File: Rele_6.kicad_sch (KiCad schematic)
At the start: 5 parts

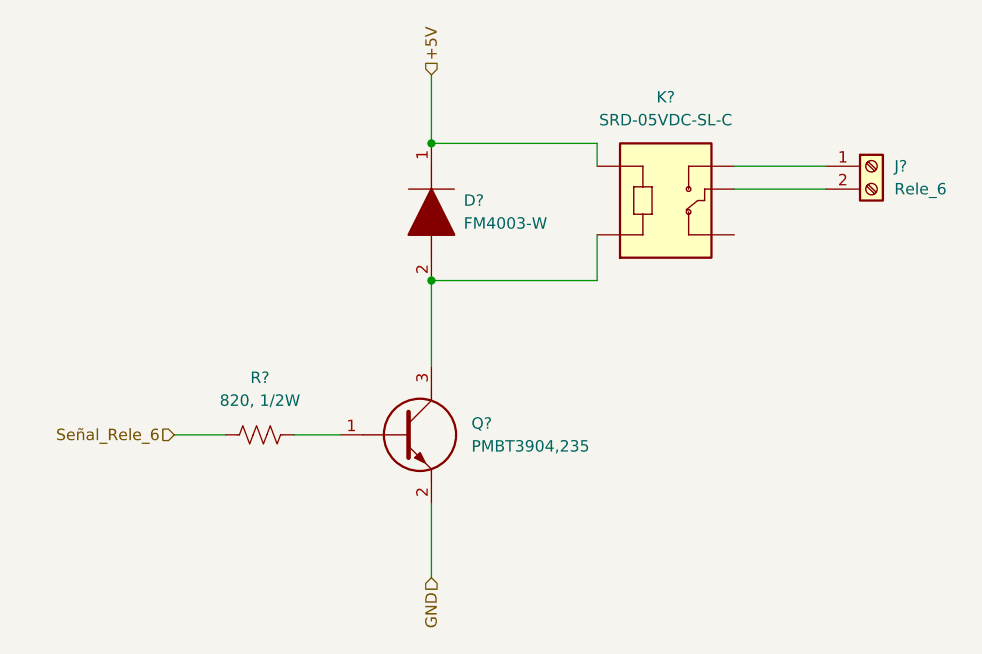
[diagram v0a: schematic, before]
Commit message: Ajuste del esquematico
Se cambio el integrado ESP32 por 2 tiras de pines de 1x15, se quitaron los switches EN y BOOT que ya estan en el NodeMCU, se quito el mutliplexor 74HC y se cablearon las I/O
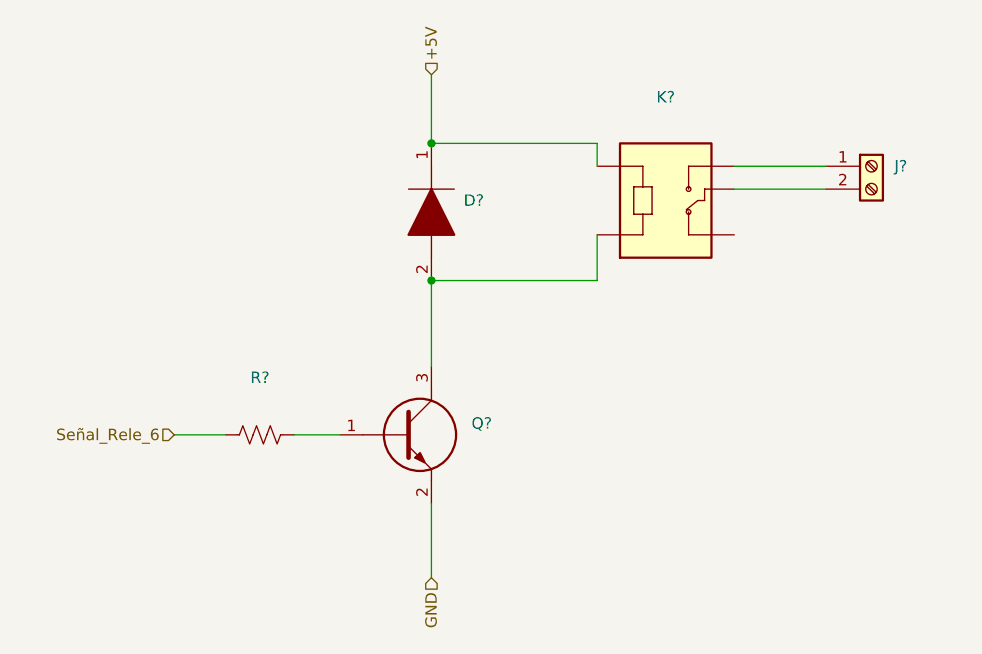
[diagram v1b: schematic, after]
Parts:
- D?: value FM4003-W -> (none); footprint DIOM5025X231N -> (none)
- J?: value Rele_6 -> (none)
- K?: value SRD-05VDC-SL-C -> (none); footprint RELAY_SRD-05VDC-SL-C -> (none)
- Q?: value PMBT3904,235 -> (none); footprint SOT95P230X110-3N -> (none)
- R?: value 820, 1/2W -> (none)
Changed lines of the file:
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@@
     (in_bom yes) (on_board yes) (fields_autoplaced)
     (property "Reference" "R?" (id 0) (at 127.635 100.965 90))
-    (property "Value" "820, 1/2W" (id 1) (at 127.635 103.505 90))
+    (property "Value" "" (id 1) (at 127.635 103.505 90))
     (property "Footprint" "" (id 2) (at 127.889 106.299 90)
       (effects (font (size 1.27 1.27)) hide)
@@
       (effects (font (size 1.27 1.27)) (justify left))
     )
-    (property "Value" "Rele_6" (id 1) (at 198.12 80.0099 0)
+    (property "Value" "" (id 1) (at 198.12 80.0099 0)
       (effects (font (size 1.27 1.27)) (justify left))
     )
@@
       (effects (font (size 1.27 1.27)) (justify left))
     )
-    (property "Value" "FM4003-W" (id 1) (at 150.2664 83.8199 90)
+    (property "Value" "" (id 1) (at 150.2664 83.8199 90)
       (effects (font (size 1.27 1.27)) (justify left))
     )
-    (property "Footprint" "DIOM5025X231N" (id 2) (at 146.685 86.36 0)
+    (property "Footprint" "" (id 2) (at 146.685 86.36 0)
       (effects (font (size 1.27 1.27)) (justify left) hide)
     )
@@
       (effects (font (size 1.27 1.27)) (justify left))
     )
-    (property "Value" "PMBT3904,235" (id 1) (at 151.13 108.5849 0)
+    (property "Value" "" (id 1) (at 151.13 108.5849 0)
       (effects (font (size 1.27 1.27)) (justify left))
     )
-    (property "Footprint" "SOT95P230X110-3N" (id 2) (at 150.495 111.125 0)
+    (property "Footprint" "" (id 2) (at 150.495 111.125 0)
       (effects (font (size 1.27 1.27)) (justify left) hide)
     )
@@
     (in_bom yes) (on_board yes) (fields_autoplaced)
     (property "Reference" "K?" (id 0) (at 172.72 69.7992 0))
-    (property "Value" "SRD-05VDC-SL-C" (id 1) (at 172.72 72.3392 0))
-    (property "Footprint" "RELAY_SRD-05VDC-SL-C" (id 2) (at 172.72 80.01 0)
+    (property "Value" "" (id 1) (at 172.72 72.3392 0))
+    (property "Footprint" "" (id 2) (at 172.72 80.01 0)
       (effects (font (size 1.27 1.27)) (justify left bottom) hide)
     )

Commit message: Modificación de posición de circ. filtrado y circ. de adaptación de tensión
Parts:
- D?, J?, K?, Q?, R?: value (none) -> ~
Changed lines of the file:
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@@
     (in_bom yes) (on_board yes) (fields_autoplaced)
     (property "Reference" "R?" (id 0) (at 127.635 100.965 90))
-    (property "Value" "" (id 1) (at 127.635 103.505 90))
+    (property "Value" "~" (id 1) (at 127.635 103.505 90))
     (property "Footprint" "" (id 2) (at 127.889 106.299 90)
       (effects (font (size 1.27 1.27)) hide)
@@
       (effects (font (size 1.27 1.27)) (justify left))
     )
-    (property "Value" "" (id 1) (at 198.12 80.0099 0)
+    (property "Value" "~" (id 1) (at 198.12 80.0099 0)
       (effects (font (size 1.27 1.27)) (justify left))
     )
@@
       (effects (font (size 1.27 1.27)) (justify left))
     )
-    (property "Value" "" (id 1) (at 150.2664 83.8199 90)
+    (property "Value" "~" (id 1) (at 150.2664 83.8199 90)
       (effects (font (size 1.27 1.27)) (justify left))
     )
@@
       (effects (font (size 1.27 1.27)) (justify left))
     )
-    (property "Value" "" (id 1) (at 151.13 108.5849 0)
+    (property "Value" "~" (id 1) (at 151.13 108.5849 0)
       (effects (font (size 1.27 1.27)) (justify left))
     )
@@
     (in_bom yes) (on_board yes) (fields_autoplaced)
     (property "Reference" "K?" (id 0) (at 172.72 69.7992 0))
-    (property "Value" "" (id 1) (at 172.72 72.3392 0))
+    (property "Value" "~" (id 1) (at 172.72 72.3392 0))
     (property "Footprint" "" (id 2) (at 172.72 80.01 0)
       (effects (font (size 1.27 1.27)) (justify left bottom) hide)

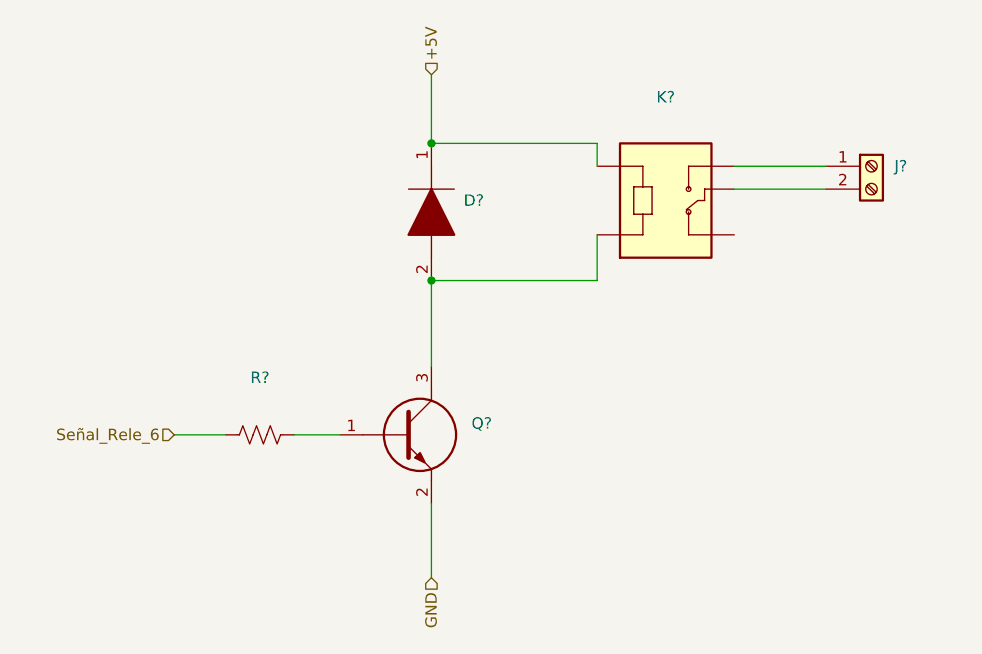
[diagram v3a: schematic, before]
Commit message: Actualización de SCH según placa industrial, y búsqueda de footprints.
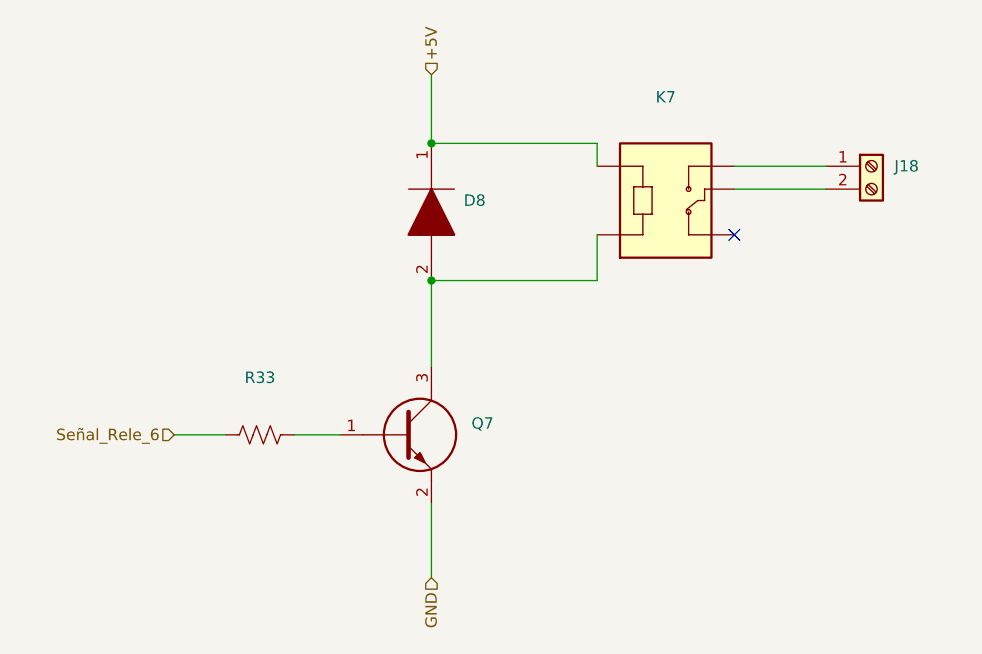
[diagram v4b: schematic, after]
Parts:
- D8: renamed from D?; value ~ -> (none)
- J18: renamed from J?; value ~ -> (none)
- K7: renamed from K?; value ~ -> (none)
- Q7: renamed from Q?; value ~ -> (none)
- R33: renamed from R?; value ~ -> (none)
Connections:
- no-connect marks 0 -> 1
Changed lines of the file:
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@@
   (junction (at 146.685 90.17) (diameter 0) (color 0 0 0 0)
   )
+  (no_connect (at 180.34 85.09))
   (wire (pts (xy 146.685 90.17) (xy 165.1 90.17))
     (stroke (width 0) (type default) (color 0 0 0 0))
@@
   (symbol (lib_id "Device:R_US") (at 127.635 107.315 90) (unit 1)
     (in_bom yes) (on_board yes) (fields_autoplaced)
-    (property "Reference" "R?" (id 0) (at 127.635 100.965 90))
-    (property "Value" "~" (id 1) (at 127.635 103.505 90))
+    (property "Reference" "R33" (id 0) (at 127.635 100.965 90))
+    (property "Value" "" (id 1) (at 127.635 103.505 90))
     (property "Footprint" "" (id 2) (at 127.889 106.299 90)
       (effects (font (size 1.27 1.27)) hide)
@@
   (symbol (lib_id "Connector:Screw_Terminal_01x02") (at 195.58 77.47 0) (unit 1)
     (in_bom yes) (on_board yes) (fields_autoplaced)
-    (property "Reference" "J?" (id 0) (at 198.12 77.4699 0)
+    (property "Reference" "J18" (id 0) (at 198.12 77.4699 0)
       (effects (font (size 1.27 1.27)) (justify left))
     )
-    (property "Value" "~" (id 1) (at 198.12 80.0099 0)
+    (property "Value" "" (id 1) (at 198.12 80.0099 0)
       (effects (font (size 1.27 1.27)) (justify left))
     )
@@
   (symbol (lib_id "FM4003-W:FM4003-W") (at 146.685 74.93 270) (unit 1)
     (in_bom yes) (on_board yes) (fields_autoplaced)
-    (property "Reference" "D?" (id 0) (at 150.2664 81.2799 90)
+    (property "Reference" "D8" (id 0) (at 150.2664 81.2799 90)
       (effects (font (size 1.27 1.27)) (justify left))
     )
-    (property "Value" "~" (id 1) (at 150.2664 83.8199 90)
+    (property "Value" "" (id 1) (at 150.2664 83.8199 90)
       (effects (font (size 1.27 1.27)) (justify left))
     )
@@
   (symbol (lib_id "PMBT3904,235:PMBT3904,235") (at 136.525 107.315 0) (unit 1)
     (in_bom yes) (on_board yes) (fields_autoplaced)
-    (property "Reference" "Q?" (id 0) (at 151.13 106.0449 0)
+    (property "Reference" "Q7" (id 0) (at 151.13 106.0449 0)
       (effects (font (size 1.27 1.27)) (justify left))
     )
-    (property "Value" "~" (id 1) (at 151.13 108.5849 0)
+    (property "Value" "" (id 1) (at 151.13 108.5849 0)
       (effects (font (size 1.27 1.27)) (justify left))
     )
@@
   (symbol (lib_id "SRD-05VDC-SL-C:SRD-05VDC-SL-C") (at 172.72 80.01 0) (unit 1)
     (in_bom yes) (on_board yes) (fields_autoplaced)
-    (property "Reference" "K?" (id 0) (at 172.72 69.7992 0))
-    (property "Value" "~" (id 1) (at 172.72 72.3392 0))
+    (property "Reference" "K7" (id 0) (at 172.72 69.7992 0))
+    (property "Value" "" (id 1) (at 172.72 72.3392 0))
     (property "Footprint" "" (id 2) (at 172.72 80.01 0)
       (effects (font (size 1.27 1.27)) (justify left bottom) hide)

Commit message: Fin de SCH, config de inicio para PCB
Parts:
- D8: value (none) -> FM4003-W; footprint (none) -> FM4003W:DIOM5025X231N
- J18: value (none) -> Rele_6; footprint (none) -> TB002-500-02BE:TB00250002BE
- K7: value (none) -> SRD-05VDC-SL-C; footprint (none) -> SRD-05VDC-SL-C-Version_2:RELAY_SRD-05VDC-SL-C
- Q7: value (none) -> PMBT3904,235; footprint (none) -> PMBT3904,235:SOT95P230X110-3N
- R33: value (none) -> 820, 1/2W; footprint (none) -> Resistor_SMD:R_0805_2012Metric
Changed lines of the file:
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@@
     (in_bom yes) (on_board yes) (fields_autoplaced)
     (property "Reference" "R33" (id 0) (at 127.635 100.965 90))
-    (property "Value" "" (id 1) (at 127.635 103.505 90))
-    (property "Footprint" "" (id 2) (at 127.889 106.299 90)
+    (property "Value" "820, 1/2W" (id 1) (at 127.635 103.505 90))
+    (property "Footprint" "Resistor_SMD:R_0805_2012Metric" (id 2) (at 127.889 106.299 90)
       (effects (font (size 1.27 1.27)) hide)
     )
@@
       (effects (font (size 1.27 1.27)) (justify left))
     )
-    (property "Value" "" (id 1) (at 198.12 80.0099 0)
+    (property "Value" "Rele_6" (id 1) (at 198.12 80.0099 0)
       (effects (font (size 1.27 1.27)) (justify left))
     )
-    (property "Footprint" "" (id 2) (at 195.58 77.47 0)
+    (property "Footprint" "TB002-500-02BE:TB00250002BE" (id 2) (at 195.58 77.47 0)
       (effects (font (size 1.27 1.27)) hide)
     )
@@
       (effects (font (size 1.27 1.27)) (justify left))
     )
-    (property "Value" "" (id 1) (at 150.2664 83.8199 90)
+    (property "Value" "FM4003-W" (id 1) (at 150.2664 83.8199 90)
       (effects (font (size 1.27 1.27)) (justify left))
     )
-    (property "Footprint" "" (id 2) (at 146.685 86.36 0)
+    (property "Footprint" "FM4003W:DIOM5025X231N" (id 2) (at 146.685 86.36 0)
       (effects (font (size 1.27 1.27)) (justify left) hide)
     )
@@
       (effects (font (size 1.27 1.27)) (justify left))
     )
-    (property "Value" "" (id 1) (at 151.13 108.5849 0)
+    (property "Value" "PMBT3904,235" (id 1) (at 151.13 108.5849 0)
       (effects (font (size 1.27 1.27)) (justify left))
     )
-    (property "Footprint" "" (id 2) (at 150.495 111.125 0)
+    (property "Footprint" "PMBT3904,235:SOT95P230X110-3N" (id 2) (at 150.495 111.125 0)
       (effects (font (size 1.27 1.27)) (justify left) hide)
     )
@@
     (in_bom yes) (on_board yes) (fields_autoplaced)
     (property "Reference" "K7" (id 0) (at 172.72 69.7992 0))
-    (property "Value" "" (id 1) (at 172.72 72.3392 0))
-    (property "Footprint" "" (id 2) (at 172.72 80.01 0)
+    (property "Value" "SRD-05VDC-SL-C" (id 1) (at 172.72 72.3392 0))
+    (property "Footprint" "SRD-05VDC-SL-C-Version_2:RELAY_SRD-05VDC-SL-C" (id 2) (at 172.72 80.01 0)
       (effects (font (size 1.27 1.27)) (justify left bottom) hide)
     )

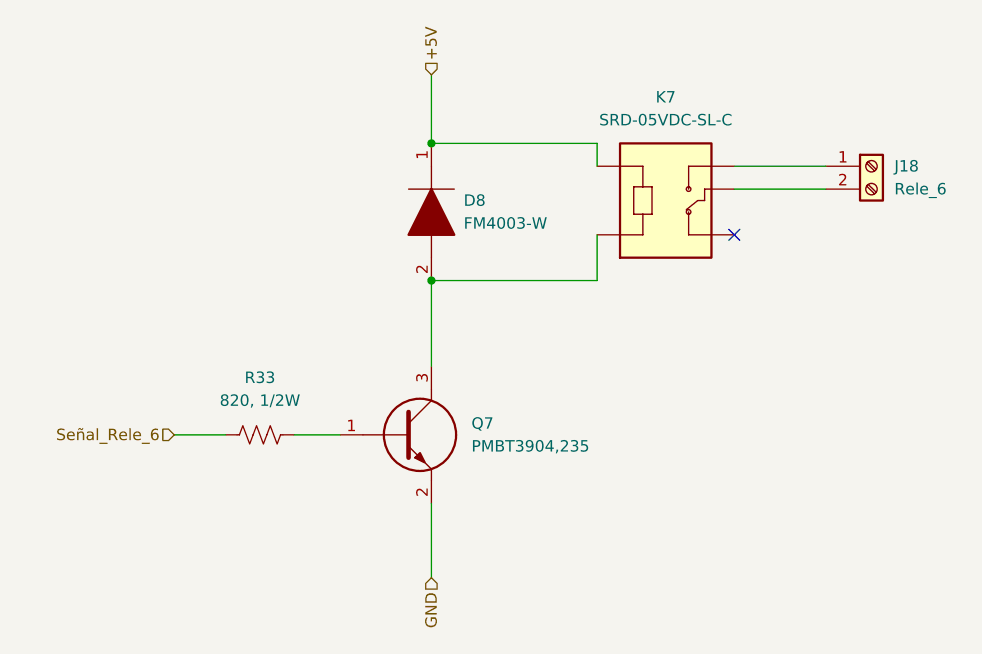
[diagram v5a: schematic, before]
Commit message: Cambios en SCH y PCB.
Se cambio el adaptador de nivel 5-3,3V por un circuito con MOSFET 2N7002, dado que ya no hay stock del NXB. Se modificó el footprint del expansor I/O por uno thorugh-hole.
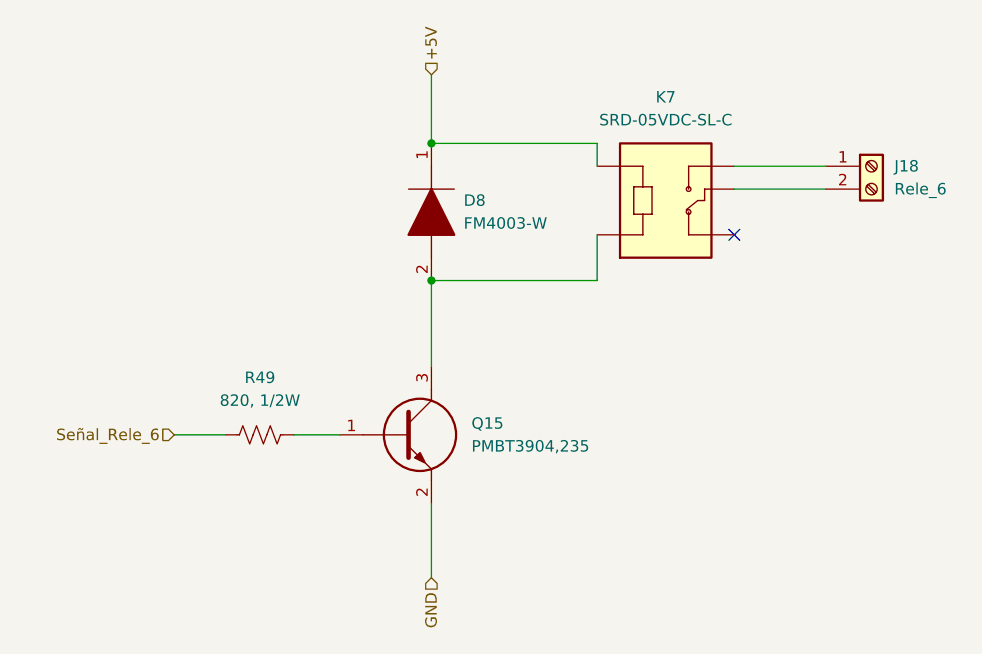
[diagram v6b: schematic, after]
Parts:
- renumbered Q7 to Q15, R33 to R49
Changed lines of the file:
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@@
   (symbol (lib_id "Device:R_US") (at 127.635 107.315 90) (unit 1)
     (in_bom yes) (on_board yes) (fields_autoplaced)
-    (property "Reference" "R33" (id 0) (at 127.635 100.965 90))
+    (property "Reference" "R49" (id 0) (at 127.635 100.965 90))
     (property "Value" "820, 1/2W" (id 1) (at 127.635 103.505 90))
     (property "Footprint" "Resistor_SMD:R_0805_2012Metric" (id 2) (at 127.889 106.299 90)
@@
   (symbol (lib_id "PMBT3904,235:PMBT3904,235") (at 136.525 107.315 0) (unit 1)
     (in_bom yes) (on_board yes) (fields_autoplaced)
-    (property "Reference" "Q7" (id 0) (at 151.13 106.0449 0)
+    (property "Reference" "Q15" (id 0) (at 151.13 106.0449 0)
       (effects (font (size 1.27 1.27)) (justify left))
     )

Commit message: Se finalizó con el PCB del prototipo.
Dado que se buscó a toda costa que el PCB fuera de 1 capa, en varios puntos del circuito se tuvieron que agregar pin headers individuales para conectar a 3V3 y GND, junto con tiras de pin headers. Cada una de estas se conectara luego entre si mediante cables.

Tambien se generaron los archivos Gerber y BOM.
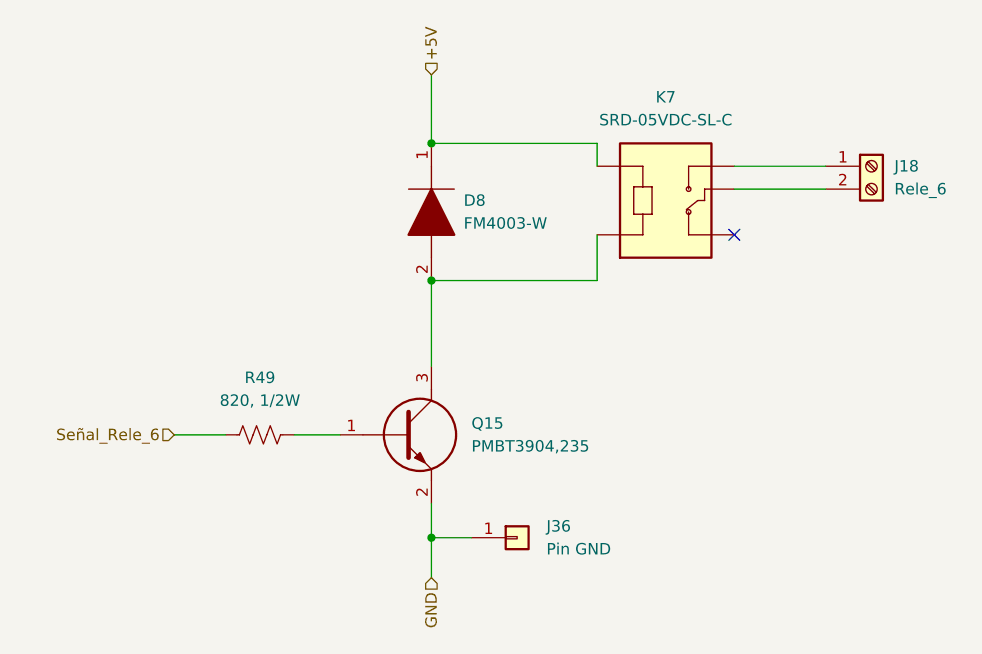
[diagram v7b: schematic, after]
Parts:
- added J36: Pin GND, Connector_PinHeader_2.54mm:PinHeader_1x01_P2.54mm_Vertical, symbol Connector_Generic:Conn_01x01
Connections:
- net GND: now also J36.1 (Pin_1)
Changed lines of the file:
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@@
 (kicad_sch (version 20211123) (generator eeschema)
   (paper "A4")
+  (junction (at 146.685 118.745) (diameter 0) (color 0 0 0 0)
+  )
   (junction (at 146.685 74.93) (diameter 0) (color 0 0 0 0)
   )
@@
     (stroke (width 0) (type default) (color 0 0 0 0))
   )
-  (wire (pts (xy 146.685 114.935) (xy 146.685 123.19))
+  (wire (pts (xy 146.685 114.935) (xy 146.685 118.745))
+    (stroke (width 0) (type default) (color 0 0 0 0))
+  )
+  (wire (pts (xy 146.685 118.745) (xy 146.685 123.19))
     (stroke (width 0) (type default) (color 0 0 0 0))
   )
@@
   )
   (wire (pts (xy 180.34 77.47) (xy 190.5 77.47))
+    (stroke (width 0) (type default) (color 0 0 0 0))
+  )
+  (wire (pts (xy 146.685 118.745) (xy 151.13 118.745))
     (stroke (width 0) (type default) (color 0 0 0 0))
   )
@@
     (pin "NO")
   )
+  (symbol (lib_id "Connector_Generic:Conn_01x01") (at 156.21 118.745 0) (unit 1)
+    (in_bom yes) (on_board yes) (fields_autoplaced)
+    (property "Reference" "J36" (id 0) (at 159.4612 117.4749 0)
+      (effects (font (size 1.27 1.27)) (justify left))
+    )
+    (property "Value" "Pin GND" (id 1) (at 159.4612 120.0149 0)
+      (effects (font (size 1.27 1.27)) (justify left))
+    )
+    (property "Footprint" "Connector_PinHeader_2.54mm:PinHeader_1x01_P2.54mm_Vertical" (id 2) (at 156.21 118.745 0)
+      (effects (font (size 1.27 1.27)) hide)
+    )
+    (property "Datasheet" "~" (id 3) (at 156.21 118.745 0)
+      (effects (font (size 1.27 1.27)) hide)
+    )
+    (pin "1")
+  )
 )
